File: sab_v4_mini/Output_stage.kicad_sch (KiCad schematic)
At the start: 50 parts, among them U14 OP275, U2 OP275

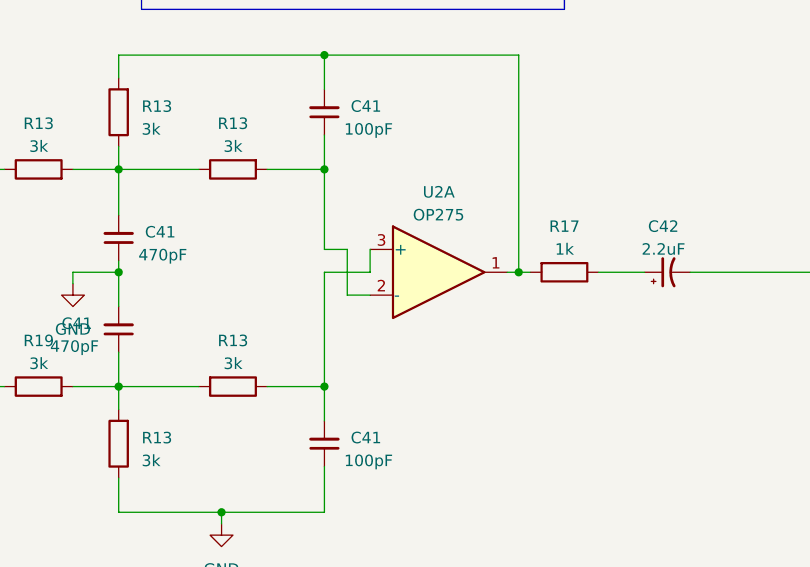
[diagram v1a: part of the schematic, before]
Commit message: added codec
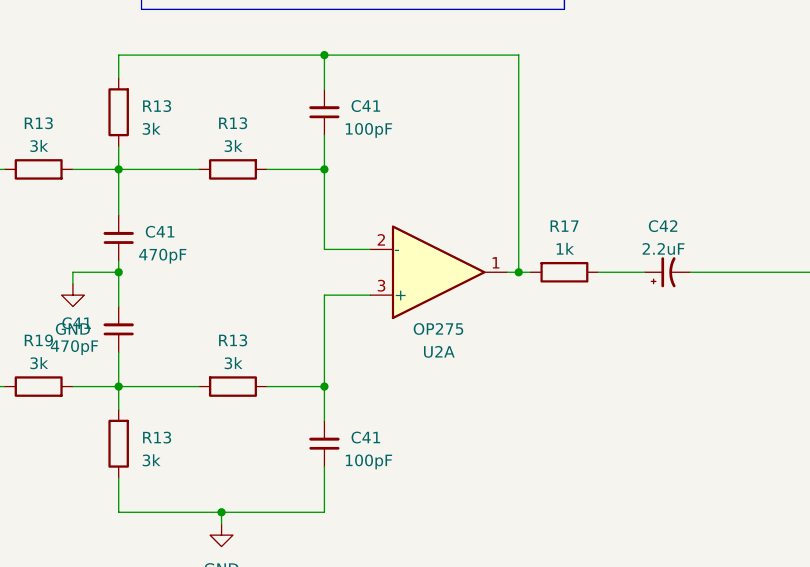
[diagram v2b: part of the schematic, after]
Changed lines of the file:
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@@
 	(wire
 		(pts
-			(xy 115.57 69.85) (xy 115.57 82.55)
+			(xy 115.57 72.39) (xy 115.57 82.55)
 		)
 		(stroke
@@
 	(wire
 		(pts
-			(xy 120.65 67.31) (xy 120.65 69.85)
-		)
-		(stroke
-			(width 0)
-			(type default)
-		)
-	)
-	(wire
-		(pts
 			(xy 262.89 132.08) (xy 262.89 137.16)
 		)
@@
 	(wire
 		(pts
-			(xy 115.57 67.31) (xy 118.11 67.31)
+			(xy 115.57 67.31) (xy 120.65 67.31)
 		)
 		(stroke
@@
 	(wire
 		(pts
-			(xy 120.65 69.85) (xy 115.57 69.85)
+			(xy 120.65 72.39) (xy 115.57 72.39)
 		)
 		(stroke
@@
 	(wire
 		(pts
-			(xy 118.11 72.39) (xy 120.65 72.39)
-		)
-		(stroke
-			(width 0)
-			(type default)
-		)
-	)
-	(wire
-		(pts
 			(xy 260.35 147.32) (xy 260.35 151.13)
 		)
@@
 	(wire
 		(pts
-			(xy 118.11 67.31) (xy 118.11 72.39)
-		)
-		(stroke
-			(width 0)
-			(type default)
-		)
-	)
-	(wire
-		(pts
 			(xy 214.63 147.32) (xy 224.79 147.32)
 		)
@@
 		(lib_id "Amplifier_Operational:OP275")
 		(at 128.27 69.85 0)
+		(mirror x)
 		(unit 1)
 		(exclude_from_sim no)
@@
 		(on_board yes)
 		(dnp no)
-		(fields_autoplaced yes)
 		(property "Reference" "U2"
-			(at 128.27 60.96 0)
+			(at 128.27 78.74 0)
 			(effects
 				(font
@@
 		)
 		(property "Value" "OP275"
-			(at 128.27 63.5 0)
+			(at 128.27 76.2 0)
 			(effects
 				(font
